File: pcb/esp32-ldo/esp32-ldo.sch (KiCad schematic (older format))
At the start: 29 parts, among them J1 BATT, J2 PROG, J3 HALL, Q1 BC817, Q2 BC807, SW1 RST, U1 XC6220, U2 ESP32-WROOM-32D

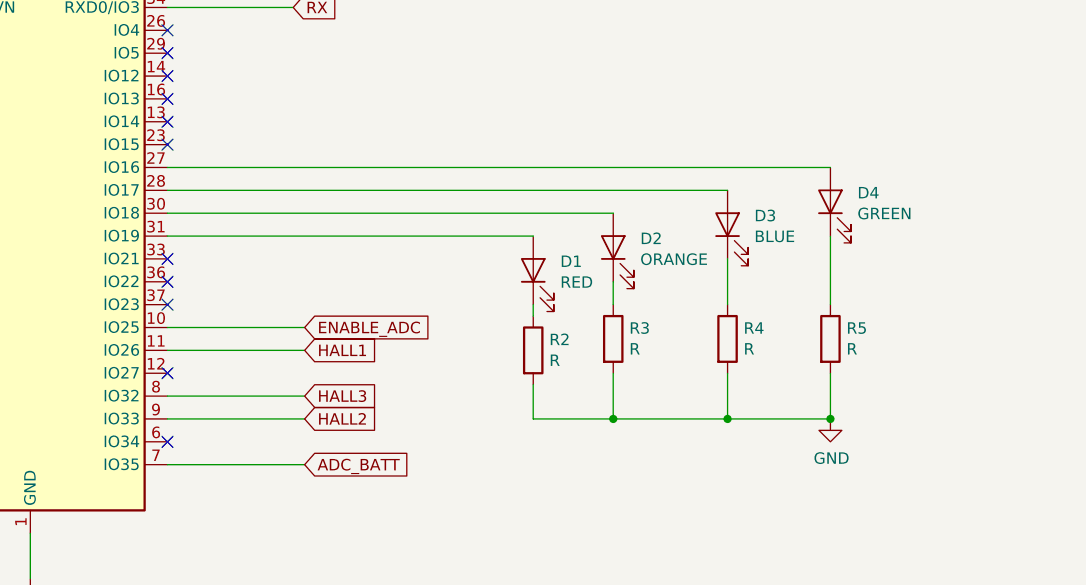
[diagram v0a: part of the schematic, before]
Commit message: pcb: removed LED 4
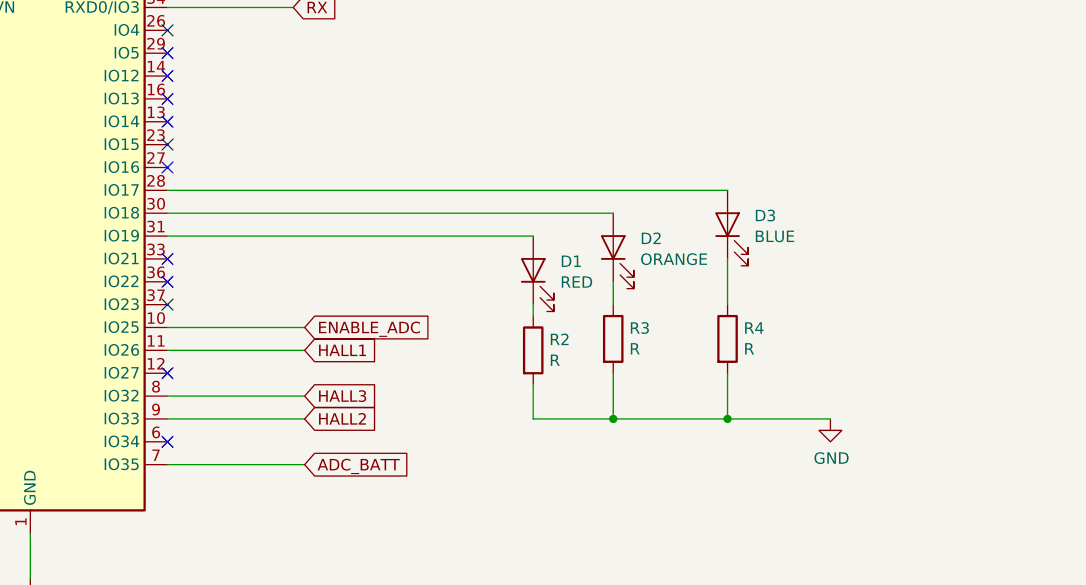
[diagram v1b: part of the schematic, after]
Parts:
- removed D4: GREEN, LED_SMD:LED_0805_2012Metric, symbol Device:LED
- removed R5: R, Resistor_SMD:R_0805_2012Metric, symbol Device:R
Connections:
- no-connect marks 20 -> 21
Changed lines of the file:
@@
-$EndComp
-$Comp
-L Device:LED D4
-U 1 1 5F20F7DF
-P 6500 3250
-F 0 "D4" V 6538 3132 50  0000 R CNN
-F 1 "GREEN" V 6447 3132 50  0000 R CNN
-F 2 "LED_SMD:LED_0805_2012Metric" H 6500 3250 50  0001 C CNN
-F 3 "~" H 6500 3250 50  0001 C CNN
-	1    6500 3250
-	0    -1   -1   0
 $EndComp
 $Comp
@@
 $EndComp
 $Comp
-L Device:R R5
-U 1 1 5F212650
-P 6500 3850
-F 0 "R5" H 6570 3896 50  0000 L CNN
-F 1 "R" H 6570 3805 50  0000 L CNN
-F 2 "Resistor_SMD:R_0805_2012Metric" V 6430 3850 50  0001 C CNN
-F 3 "~" H 6500 3850 50  0001 C CNN
-	1    6500 3850
-	1    0    0    -1
-$EndComp
-$Comp
 L power:GND #PWR014
 U 1 1 5F21269A
@@
 	1    0    0    -1
 $EndComp
-Wire Wire Line
-	6500 3700 6500 3400
 Wire Wire Line
 	6050 3500 6050 3700
@@
 	6050 4200 5550 4200
 Wire Wire Line
-	6500 4000 6500 4200
-Connection ~ 6500 4200
-Wire Wire Line
 	5200 3400 3600 3400
 Wire Wire Line
 	3600 3200 6050 3200
-Wire Wire Line
-	6500 3100 3600 3100
 Wire Wire Line
 	5200 3700 5200 3750
@@
 Wire Wire Line
 	10650 1150 10400 1150
+NoConn ~ 3600 3100
 $EndSCHEMATC
